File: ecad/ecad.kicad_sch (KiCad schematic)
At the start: 0 parts

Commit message: chore (ecad): Config paper sizes
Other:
- title: (none) -> ESP32 AK Shield Schematik drawing
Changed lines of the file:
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@@
 	(generator "eeschema")
 	(generator_version "9.0")
-	(paper "A4")
+	(paper "A5")
+	(title_block
+		(title "ESP32 AK Shield Schematik drawing")
+		(date "2025-12-18")
+		(rev "A")
+	)
 	(sheet_instances
 		(path "/"

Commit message: chore (ecad): init PCB & Schematic
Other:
- added sheet ESP32 CAM (esp32-cam.kicad_sch)
- added sheet ESP32 CH340 (esp32-ch340.kicad_sch)
- added sheet ESP32 CP2102 (esp32-cp2102.kicad_sch)
- added sheet ESP32 S3 (esp32-s3.kicad_sch)
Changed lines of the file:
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@@
 	(generator "eeschema")
 	(generator_version "9.0")
-	(paper "A5")
+	(paper "A5" portrait)
 	(title_block
 		(title "ESP32 AK Shield Schematik drawing")
@@
 		(rev "A")
 	)
+	(sheet
+		(at 13.97 16.51)
+		(size 49.53 3.81)
+		(exclude_from_sim no)
+		(in_bom yes)
+		(on_board yes)
+		(dnp no)
+		(fields_autoplaced yes)
+		(stroke
+			(width 0.1524)
+			(type solid)
+		)
+		(fill
+			(color 0 0 0 0.0000)
+		)
+		(property "Sheetname" "ESP32 CAM"
+			(at 13.97 15.7984 0)
+			(effects
+				(font
+					(size 1.27 1.27)
+				)
+				(justify left bottom)
+			)
+		)
+		(property "Sheetfile" "esp32-cam.kicad_sch"
+			(at 13.97 20.9046 0)
+			(effects
+				(font
+					(size 1.27 1.27)
+				)
+				(justify left top)
+			)
+		)
+		(instances
+			(project "ecad"
+				(path "/a5f24e88-7373-4c84-afe0-8843cd13fbc2"
+					(page "2")
+				)
+			)
+		)
+	)
+	(sheet
+		(at 13.97 46.99)
+		(size 49.53 3.81)
+		(exclude_from_sim no)
+		(in_bom yes)
+		(on_board yes)
+		(dnp no)
+		(fields_autoplaced yes)
+		(stroke
+			(width 0.1524)
+			(type solid)
+		)
+		(fill
+			(color 0 0 0 0.0000)
+		)
+		(property "Sheetname" "ESP32 S3"
+			(at 13.97 46.2784 0)
+			(effects
+				(font
+					(size 1.27 1.27)
+				)
+				(justify left bottom)
+			)
+		)
+		(property "Sheetfile" "esp32-s3.kicad_sch"
+			(at 13.97 51.3846 0)
+			(effects
+				(font
+					(size 1.27 1.27)
+				)
+				(justify left top)
+			)
+		)
+		(instances
+			(project "ecad"
+				(path "/a5f24e88-7373-4c84-afe0-8843cd13fbc2"
+					(page "5")
+				)
+			)
+		)
+	)
+	(sheet
+		(at 13.97 36.83)
+		(size 49.53 3.81)
+		(exclude_from_sim no)
+		(in_bom yes)
+		(on_board yes)
+		(dnp no)
+		(fields_autoplaced yes)
+		(stroke
+			(width 0.1524)
+			(type solid)
+		)
+		(fill
+			(color 0 0 0 0.0000)
+		)
+		(property "Sheetname" "ESP32 CP2102"
+			(at 13.97 36.1184 0)
+			(effects
+				(font
+					(size 1.27 1.27)
+				)
+				(justify left bottom)
+			)
+		)
+		(property "Sheetfile" "esp32-cp2102.kicad_sch"
+			(at 13.97 41.2246 0)
+			(effects
+				(font
+					(size 1.27 1.27)
+				)
+				(justify left top)
+			)
+		)
+		(instances
+			(project "ecad"
+				(path "/a5f24e88-7373-4c84-afe0-8843cd13fbc2"
+					(page "4")
+				)
+			)
+		)
+	)
+	(sheet
+		(at 13.97 26.67)
+		(size 49.53 3.81)
+		(exclude_from_sim no)
+		(in_bom yes)
+		(on_board yes)
+		(dnp no)
+		(fields_autoplaced yes)
+		(stroke
+			(width 0.1524)
+			(type solid)
+		)
+		(fill
+			(color 0 0 0 0.0000)
+		)
+		(property "Sheetname" "ESP32 CH340"
+			(at 13.97 25.9584 0)
+			(effects
+				(font
+					(size 1.27 1.27)
+				)
+				(justify left bottom)
+			)
+		)
+		(property "Sheetfile" "esp32-ch340.kicad_sch"
+			(at 13.97 31.0646 0)
+			(effects
+				(font
+					(size 1.27 1.27)
+				)
+				(justify left top)
+			)
+		)
+		(instances
+			(project "ecad"
+				(path "/a5f24e88-7373-4c84-afe0-8843cd13fbc2"
+					(page "3")
+				)
+			)
+		)
+	)
 	(sheet_instances

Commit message: feat (ecad): update KiCad project
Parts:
- added C1, C2, C4: 100n, Capacitor_SMD:C_0805_2012Metric_Pad1.18x1.45mm_HandSolder, symbol Device:C
- added C3: 1u, Capacitor_SMD:CP_Elec_4x5.4, symbol Device:C_Polarized_US
- added C5: 4.7u, Capacitor_SMD:CP_Elec_4x5.4, symbol Device:C_Polarized_US
- added C6, C7: 22u, Capacitor_SMD:C_0805_2012Metric_Pad1.18x1.45mm_HandSolder, symbol Device:C
- added C8, C9: 470u, Capacitor_SMD:CP_Elec_8x10.5, symbol Device:C_Polarized_US
- added D55: SM4001, Diode_SMD:D_MELF, symbol Diode:SM4001
- added D57: SS34, Diode_SMD:D_SMA, symbol Diode:SS34
- added J1, J2, J4, J5, J6, J7: Conn_01x22_Pin, Connector_PinHeader_2.54mm:PinHeader_1x22_P2.54mm_Vertical, symbol Connector:Conn_01x22_Pin
- added J3: USB_C, Connector_USB:USB_C_Receptacle_Palconn_UTC16-G, symbol Connector:USB_C_Receptacle_USB2.0_16P
- added J8, J9: Conn_01x03_Pin, Connector_PinHeader_2.54mm:PinHeader_1x03_P2.54mm_Vertical, symbol Connector:Conn_01x03_Pin
- added L1: 33u, Inductor_SMD:L_6.3x6.3_H3, symbol Device:L
- added R55: 10k, Resistor_SMD:R_0805_2012Metric_Pad1.20x1.40mm_HandSolder, symbol Device:R_US
- added U11: FT232RL, Package_SO:SSOP-28_5.3x10.2mm_P0.65mm, symbol Interface_USB:FT232RL
- added U16: AMS1117-3.3, Package_TO_SOT_SMD:SOT-223-3_TabPin2, symbol Regulator_Linear:AMS1117-3.3
- added U17: LM2596S-ADJ, Package_TO_SOT_SMD:TO-263-5_TabPin3, symbol Regulator_Switching:LM2596S-ADJ
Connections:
- new net: R55.1, U11.14 (CBUS3)
- new net: D57.1 (K), L1.1, U17.2 (OUT)
- new net +12V: C8.1, U17.1 (VIN)
- new net +3.3V: C2.1, C7.1, J8.3 (Pin_3), J9.3 (Pin_3), U11.17 (3V3OUT), U16.2 (VO)
- new net +5V: C4.1, C5.1, C6.1, C9.1, D55.1 (K), J8.1 (Pin_1), J9.1 (Pin_1), L1.2, U11.20 (VCC), U16.3 (VI), U17.4 (FB)
- new net CAM_GPIO00: J2.2 (Pin_2)
- new net CAM_GPIO01: J2.4 (Pin_4)
- new net CAM_GPIO02: J1.5 (Pin_5)
- new net CAM_GPIO03: J2.3 (Pin_3)
- new net CAM_GPIO04: J1.10 (Pin_10), J1.12 (Pin_12), J1.13 (Pin_13), J1.15 (Pin_15), J1.16 (Pin_16), J1.18 (Pin_18), J1.19 (Pin_19), J1.20 (Pin_20), J1.6 (Pin_6), J1.7 (Pin_7), J1.9 (Pin_9)
- new net CAM_GPIO12: J1.1 (Pin_1)
- new net CAM_GPIO13: J1.2 (Pin_2)
- new net CAM_GPIO14: J1.4 (Pin_4)
- new net CAM_GPIO15: J1.3 (Pin_3)
- new net CAM_GPIO16: J2.1 (Pin_1)
- new net Earth: C1.2, C2.2, C3.2, C4.2, C5.2, C6.2, C7.2, C8.2, C9.2, D57.2 (A), J3.A1 (GND), J3.A12 (GND), J3.B1 (GND), J3.B12 (GND), J3.S1 (SHIELD), J5.1 (Pin_1), J5.10 (Pin_10), J5.11 (Pin_11), J5.12 (Pin_12), J5.13 (Pin_13), J5.14 (Pin_14), J5.15 (Pin_15), J5.16 (Pin_16), J5.17 (Pin_17), J5.18 (Pin_18), J5.19 (Pin_19), J5.2 (Pin_2), J5.20 (Pin_20), J5.21 (Pin_21), J5.22 (Pin_22), J5.3 (Pin_3), J5.4 (Pin_4), J5.5 (Pin_5), J5.6 (Pin_6), J5.7 (Pin_7), J5.8 (Pin_8), J5.9 (Pin_9), J6.1 (Pin_1), J6.10 (Pin_10), J6.11 (Pin_11), J6.12 (Pin_12), J6.13 (Pin_13), J6.14 (Pin_14), J6.15 (Pin_15), J6.16 (Pin_16), J6.17 (Pin_17), J6.18 (Pin_18), J6.19 (Pin_19), J6.2 (Pin_2), J6.20 (Pin_20), J6.21 (Pin_21), J6.22 (Pin_22), J6.3 (Pin_3), J6.4 (Pin_4), J6.5 (Pin_5), J6.6 (Pin_6), J6.7 (Pin_7), J6.8 (Pin_8), J6.9 (Pin_9), U11.18 (GND), U11.21 (GND), U11.25 (AGND), U11.26 (TEST), U11.7 (GND), U16.1 (GND), U17.3 (GND), U17.5 (~{ON}/OFF)
- new net FLASH_CMD: J1.21 (Pin_21)
- new net FLASH_D0: J2.21 (Pin_21)
- new net FLASH_D1: J2.12 (Pin_12), J2.14 (Pin_14), J2.16 (Pin_16), J2.18 (Pin_18), J2.19 (Pin_19), J2.20 (Pin_20), J2.6 (Pin_6), J2.9 (Pin_9)
- new net FLASH_SCK: J2.22 (Pin_22)
- new net GPIO00: J2.11 (Pin_11), J2.13 (Pin_13), J2.15 (Pin_15), J2.17 (Pin_17), J2.5 (Pin_5), J2.8 (Pin_8)
- new net GPIO01: J2.10 (Pin_10), J2.7 (Pin_7)
- new net GPIO27: J1.11 (Pin_11), J1.14 (Pin_14), J1.17 (Pin_17), J1.8 (Pin_8)
- new net RX0: U11.5 (RXD)
- new net TX0: U11.1 (TXD)
- new net USBD_+: J3.A6 (D+), J3.B6 (D+), U11.15 (USBD+)
- new net USBD_-: J3.A7 (D-), J3.B7 (D-), U11.16 (USBD-)
- new net VBUS: C3.1, D55.2 (A), J3.A4 (VBUS), J3.A9 (VBUS), J3.B4 (VBUS), J3.B9 (VBUS)
- new net VCC: J4.1 (Pin_1), J4.10 (Pin_10), J4.11 (Pin_11), J4.12 (Pin_12), J4.13 (Pin_13), J4.14 (Pin_14), J4.15 (Pin_15), J4.16 (Pin_16), J4.17 (Pin_17), J4.18 (Pin_18), J4.19 (Pin_19), J4.2 (Pin_2), J4.20 (Pin_20), J4.21 (Pin_21), J4.22 (Pin_22), J4.3 (Pin_3), J4.4 (Pin_4), J4.5 (Pin_5), J4.6 (Pin_6), J4.7 (Pin_7), J4.8 (Pin_8), J4.9 (Pin_9), J7.1 (Pin_1), J7.10 (Pin_10), J7.11 (Pin_11), J7.12 (Pin_12), J7.13 (Pin_13), J7.14 (Pin_14), J7.15 (Pin_15), J7.16 (Pin_16), J7.17 (Pin_17), J7.18 (Pin_18), J7.19 (Pin_19), J7.2 (Pin_2), J7.20 (Pin_20), J7.21 (Pin_21), J7.22 (Pin_22), J7.3 (Pin_3), J7.4 (Pin_4), J7.5 (Pin_5), J7.6 (Pin_6), J7.7 (Pin_7), J7.8 (Pin_8), J7.9 (Pin_9), J8.2 (Pin_2)
- new net Vdrive: C1.1, J9.2 (Pin_2), R55.2, U11.4 (VCCIO)
- no-connect marks 0 -> 18
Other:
- added sheet LEDS (leds.kicad_sch)
- title: ESP32 AK Shield Schematik drawing -> ESP32 AK Shield Schematik drawing ROOT

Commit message: feat (ecad): update KiCad project
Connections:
- net GPIO00 is gone; now on net CAM_GPIO03: J2.11 (Pin_11), J2.13 (Pin_13), J2.15 (Pin_15), J2.17 (Pin_17), J2.5 (Pin_5), J2.8 (Pin_8)
- net GPIO01 is gone; now on net CAM_GPIO00: J2.10 (Pin_10), J2.7 (Pin_7)
- net RX0 is gone; now on net CAM_GPIO03: U11.5 (RXD)
- net TX0 is gone; now on net CAM_GPIO00: U11.1 (TXD)
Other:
- moved on the sheet: C2, C6, C7, C8, C9, D57, L1, R55, U11, U16, U17

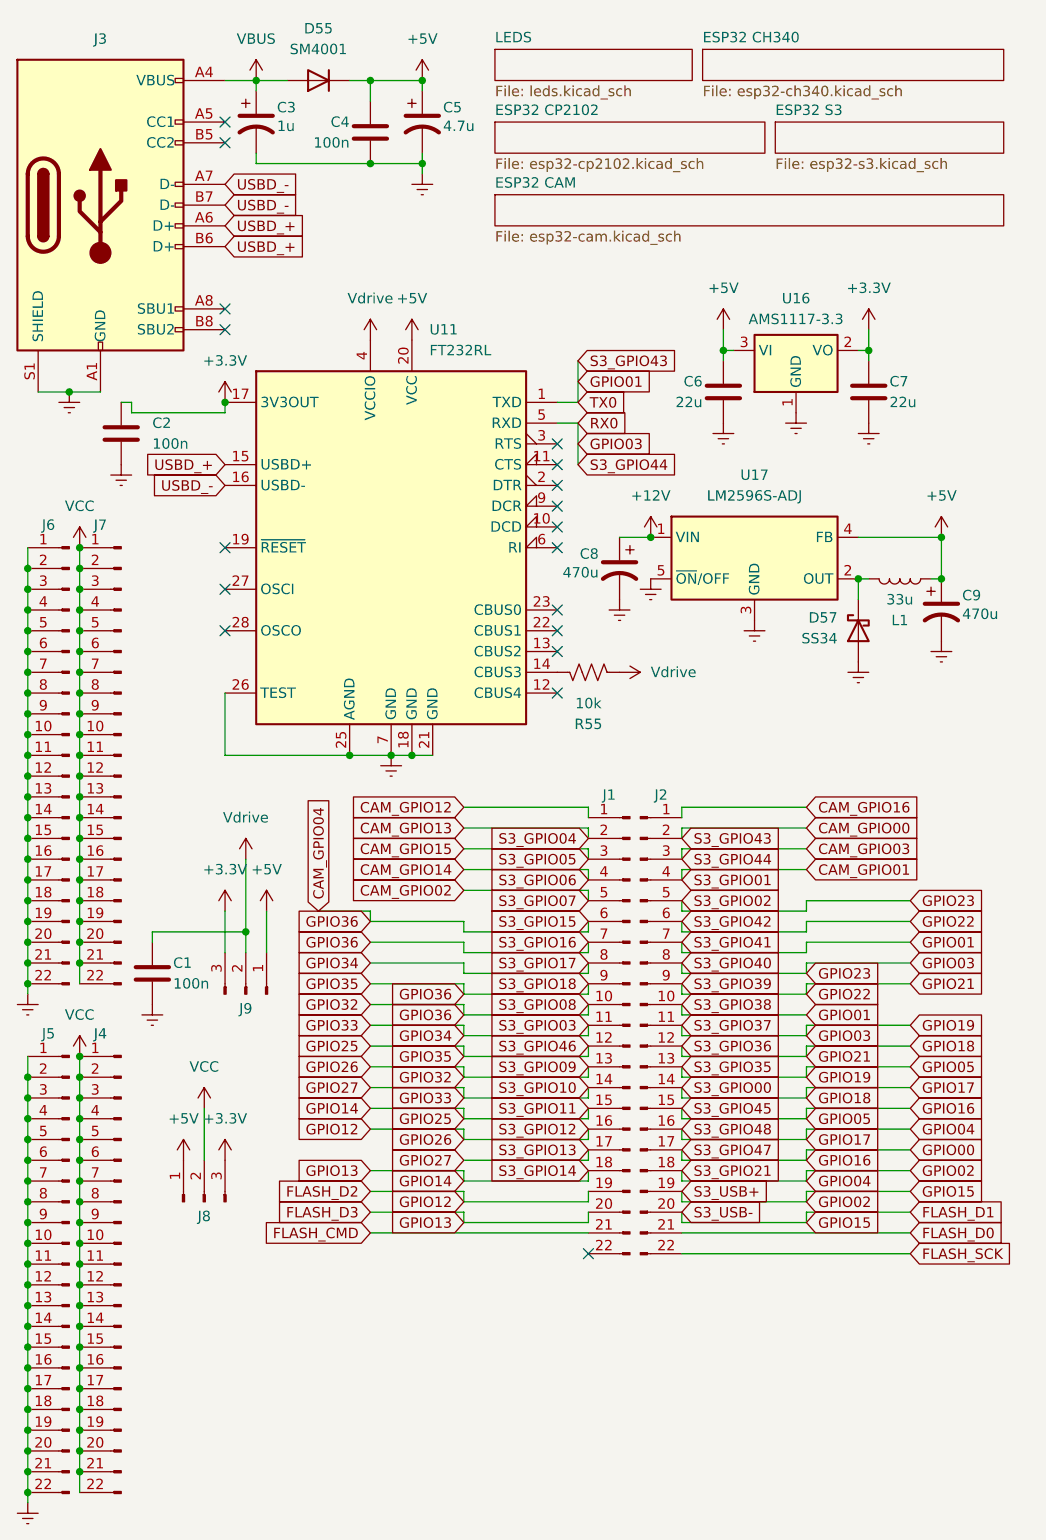
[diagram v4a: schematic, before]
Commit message: feat (ecad): start PCB design
Left header pins and LEDs connected to devkits without ground-voltage
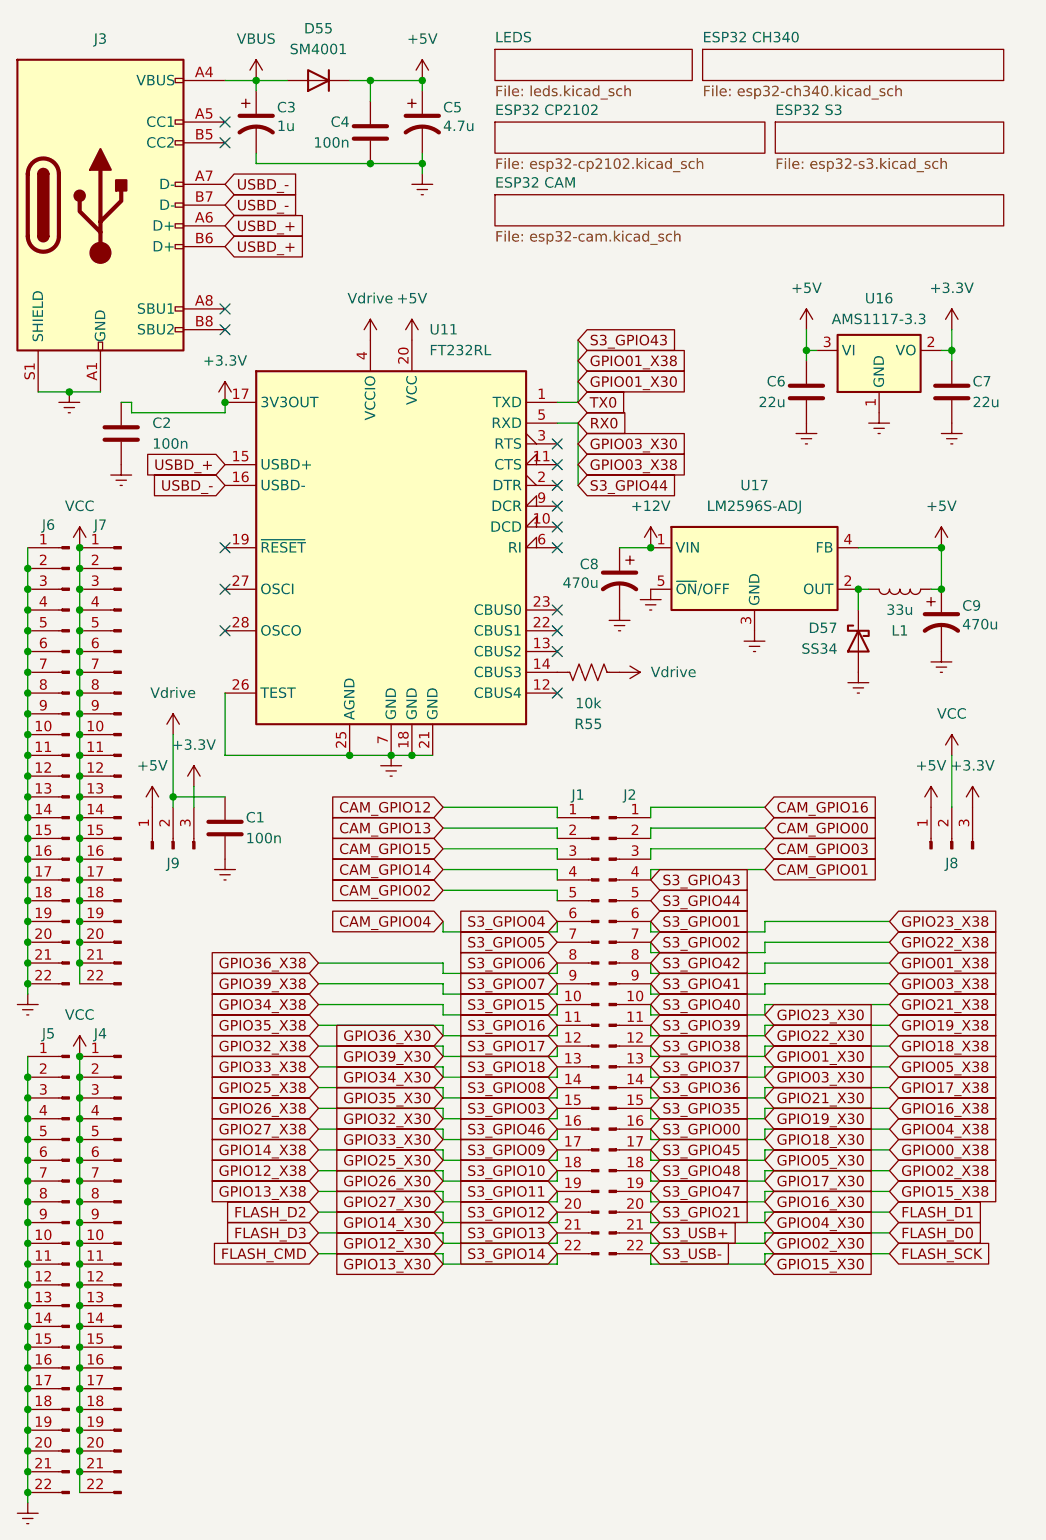
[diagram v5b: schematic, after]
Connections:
- net CAM_GPIO00: no longer J2.10 (Pin_10), J2.7 (Pin_7), U11.1 (TXD)
- net CAM_GPIO01: now also J2.12 (Pin_12), J2.8 (Pin_8), U11.1 (TXD)
- net CAM_GPIO03: no longer J2.11 (Pin_11), J2.13 (Pin_13), J2.15 (Pin_15), J2.17 (Pin_17), J2.5 (Pin_5), J2.8 (Pin_8), U11.5 (RXD)
- net CAM_GPIO04: no longer J1.10 (Pin_10), J1.12 (Pin_12), J1.13 (Pin_13), J1.15 (Pin_15), J1.16 (Pin_16), J1.18 (Pin_18), J1.19 (Pin_19), J1.20 (Pin_20), J1.7 (Pin_7), J1.9 (Pin_9)
- net FLASH_CMD: now also J1.22 (Pin_22); no longer J1.21 (Pin_21)
- net FLASH_D1: no longer J2.12 (Pin_12), J2.14 (Pin_14), J2.16 (Pin_16), J2.18 (Pin_18), J2.19 (Pin_19), J2.6 (Pin_6), J2.9 (Pin_9)
- removed net GPIO27: J1.11 (Pin_11), J1.14 (Pin_14), J1.17 (Pin_17), J1.8 (Pin_8)
- new net FLASH_D2: J1.20 (Pin_20)
- new net FLASH_D3: J1.21 (Pin_21)
- new net GPIO00_X38: J2.17 (Pin_17)
- new net GPIO02_X38: J2.18 (Pin_18)
- new net GPIO03_X30: J2.13 (Pin_13), J2.5 (Pin_5), J2.9 (Pin_9), U11.5 (RXD)
- new net GPIO04_X38: J2.16 (Pin_16)
- new net GPIO12_X38: J1.18 (Pin_18)
- new net GPIO13_X38: J1.19 (Pin_19)
- new net GPIO14_X38: J1.17 (Pin_17)
- new net GPIO15_X38: J2.19 (Pin_19)
- new net GPIO16_X38: J2.15 (Pin_15)
- new net GPIO17_X38: J2.14 (Pin_14)
- new net GPIO19_X38: J2.11 (Pin_11)
- new net GPIO21_X38: J2.10 (Pin_10)
- new net GPIO22_X38: J2.7 (Pin_7)
- new net GPIO23_X38: J2.6 (Pin_6)
- new net GPIO25_X38: J1.14 (Pin_14)
- new net GPIO26_X38: J1.15 (Pin_15)
- new net GPIO27_X38: J1.16 (Pin_16)
- new net GPIO32_X38: J1.12 (Pin_12)
- new net GPIO33_X38: J1.13 (Pin_13)
- new net GPIO34_X38: J1.10 (Pin_10)
- new net GPIO35_X38: J1.11 (Pin_11)
- new net GPIO36_X38: J1.8 (Pin_8)
- new net GPIO39_X38: J1.9 (Pin_9)
- new net S3_GPIO05: J1.7 (Pin_7)
- no-connect marks 18 -> 17
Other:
- moved on the sheet: C1, C6, C7, C8, C9, D57, J1, J2, J8, J9, L1, U16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

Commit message: feat (ecad): update PCB design
header pins and LEDs connected to devkits without ground-voltage
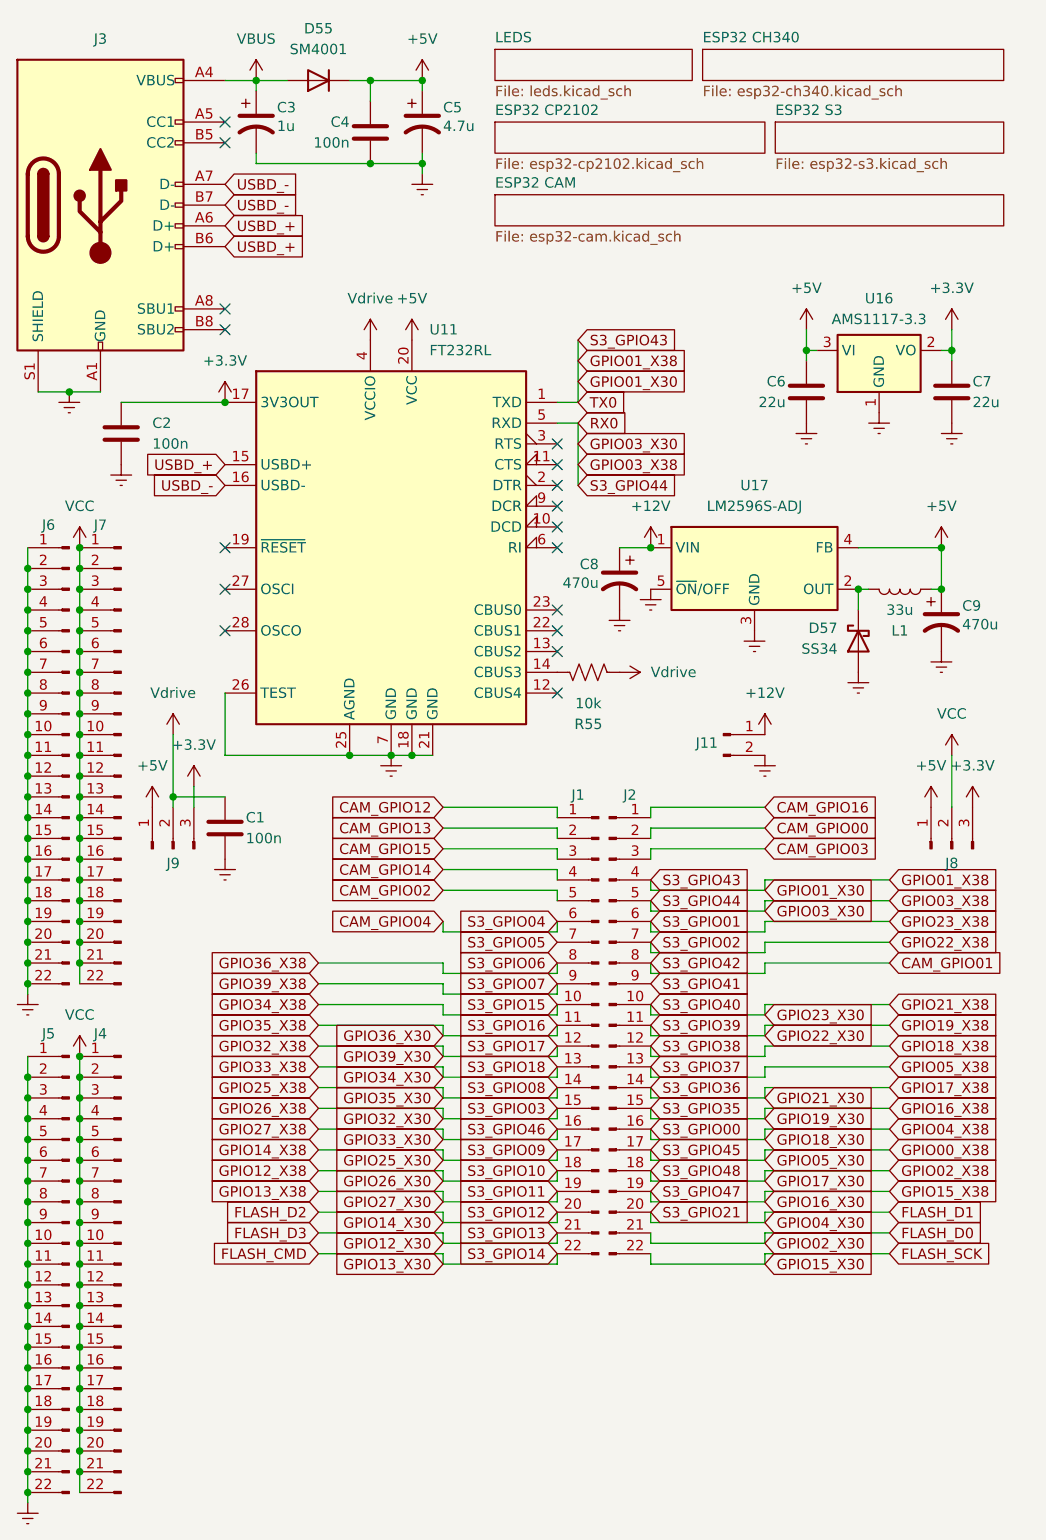
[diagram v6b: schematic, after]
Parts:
- added J11: Conn_01x02_Pin, Connector_BarrelJack:BarrelJack_GCT_DCJ200-10-A_Horizontal, symbol Connector:Conn_01x02_Pin
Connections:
- net +12V: now also J11.1 (Pin_1)
- net CAM_GPIO01: no longer J2.12 (Pin_12), J2.4 (Pin_4), U11.1 (TXD)
- net Earth: now also J11.2 (Pin_2)
- net GPIO03_X30: no longer J2.13 (Pin_13), J2.9 (Pin_9)
- new net GPIO01_X30: J2.4 (Pin_4), U11.1 (TXD)
- new net GPIO05_X38: J2.13 (Pin_13)
- new net GPIO18_X38: J2.12 (Pin_12)
- new net S3_GPIO41: J2.9 (Pin_9)
